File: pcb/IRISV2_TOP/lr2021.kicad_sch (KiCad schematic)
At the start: 52 parts, among them J7 Conn_Coaxial, J8 Conn_Coaxial, U9 lr2021, Y5 ECS-TXO-32CSMV-320-AN-TR

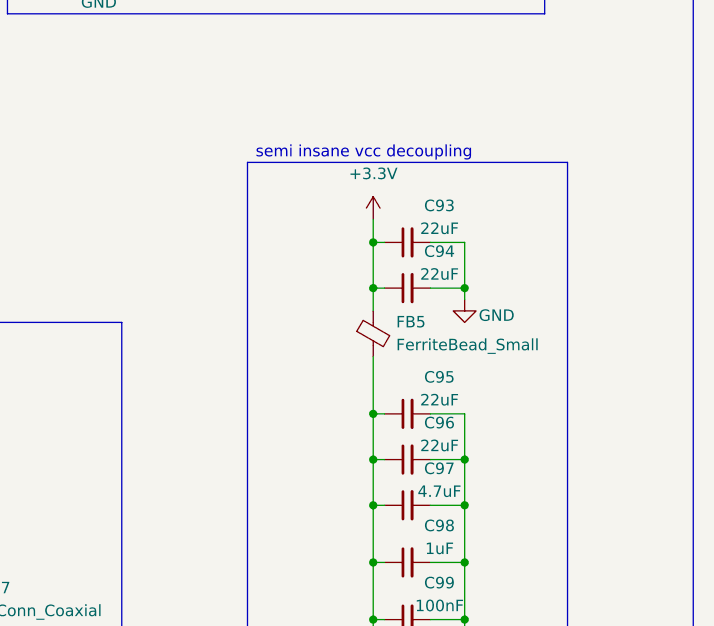
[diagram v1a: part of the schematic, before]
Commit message: removed high g accel, top board layout looking decent, routing started also - though i realized i was missing the micro sd card and that's going to be a pain to add
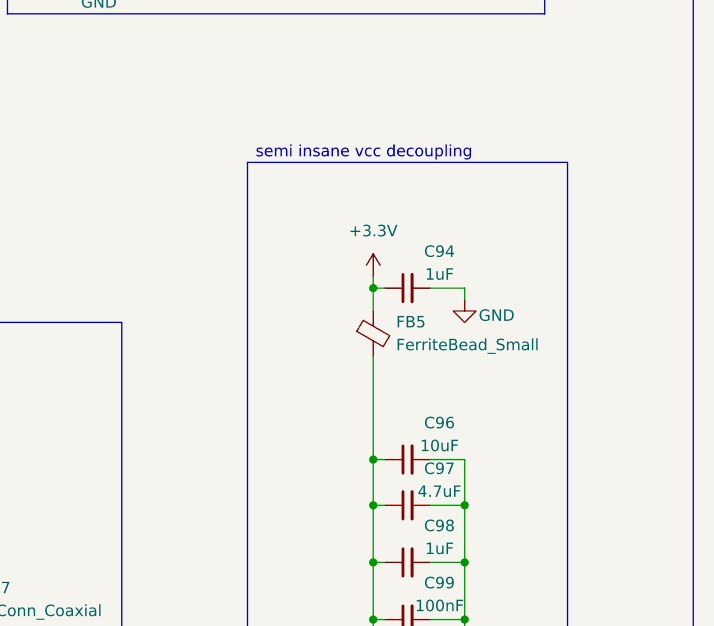
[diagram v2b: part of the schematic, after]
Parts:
- removed C93, C95: 22uF, Capacitor_SMD:C_1210_3225Metric, symbol Device:C_Small
- C80, C81: footprint Capacitor_SMD:C_0805_2012Metric -> Capacitor_SMD:C_0603_1608Metric
- C94: value 22uF -> 1uF; footprint Capacitor_SMD:C_1210_3225Metric -> Capacitor_SMD:C_0603_1608Metric
- C96: value 22uF -> 10uF; footprint Capacitor_SMD:C_1210_3225Metric -> Capacitor_SMD:C_0603_1608Metric
- D7, D8: footprint (none) -> Diode_SMD:D_0201_0603Metric
- FB3, FB4, FB5: footprint (none) -> Inductor_SMD:L_0402_1005Metric

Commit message: layout pretty much done, lr2021 rf stuff done, mostly just routing left
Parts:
- C74, C85: footprint Capacitor_SMD:C_0402_1005Metric -> Capacitor_SMD:C_0201_0603Metric
- J7, J8: footprint (none) -> Connector_Coaxial:U.FL_Hirose_U.FL-R-SMT-1_Vertical
- U9: footprint LR2021:LR2021 -> LR2021:LR2021_thermalvias
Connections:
- net hf: now reaches C92.1, D8.2 (A2), J8.1 (In), L14.2, L15.1
- net hf: no longer C86.2
- net hf_tiein: now reaches C90.2, C91.1, L13.2, L14.1
- net hf_tiein: now also C86.2
- net lf: now reaches C75.2, C82.1, D7.2 (A2), J7.1 (In), L7.2, L9.1
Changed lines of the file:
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@@
 	)
 	(junction
+		(at 119.38 50.8)
+		(diameter 0)
+		(color 0 0 0 0)
+	)
+	(junction
 		(at 119.38 54.61)
 		(diameter 0)
@@
 	(wire
 		(pts
+			(xy 106.68 31.75) (xy 119.38 31.75)
+		)
+		(stroke
+			(width 0)
+			(type default)
+		)
+	)
+	(wire
+		(pts
 			(xy 97.79 31.75) (xy 99.06 31.75)
 		)
@@
 	(wire
 		(pts
-			(xy 129.54 31.75) (xy 129.54 54.61)
-		)
-		(stroke
-			(width 0)
-			(type default)
-		)
-	)
-	(wire
-		(pts
 			(xy 67.31 176.53) (xy 67.31 177.8)
 		)
@@
 	(wire
 		(pts
+			(xy 119.38 31.75) (xy 119.38 50.8)
+		)
+		(stroke
+			(width 0)
+			(type default)
+		)
+	)
+	(wire
+		(pts
 			(xy 138.43 142.24) (xy 139.7 142.24)
 		)
@@
 	(wire
 		(pts
-			(xy 106.68 31.75) (xy 129.54 31.75)
-		)
-		(stroke
-			(width 0)
-			(type default)
-		)
-	)
-	(wire
-		(pts
 			(xy 40.64 35.56) (xy 40.64 36.83)
 		)
@@
 		)
 	)
+	(label "hf"
+		(at 146.05 54.61 0)
+		(effects
+			(font
+				(size 1.27 1.27)
+			)
+			(justify left bottom)
+		)
+	)
 	(label "lfo"
 		(at 25.4 176.53 180)
@@
 		)
 	)
+	(label "lf"
+		(at 83.82 176.53 0)
+		(effects
+			(font
+				(size 1.27 1.27)
+			)
+			(justify left bottom)
+		)
+	)
 	(label "lr2021_vpax"
 		(at 38.1 58.42 90)
@@
 		)
 	)
+	(label "hf_tiein"
+		(at 113.03 31.75 0)
+		(effects
+			(font
+				(size 1.27 1.27)
+			)
+			(justify left bottom)
+		)
+	)
 	(label "lr_vtcxo"
 		(at 24.13 73.66 180)
@@
 			)
 		)
-		(property "Footprint" "Capacitor_SMD:C_0402_1005Metric"
+		(property "Footprint" "Capacitor_SMD:C_0201_0603Metric"
 			(at 36.5252 162.56 0)
 			(effects
@@
 			)
 		)
-		(property "Footprint" ""
+		(property "Footprint" "Connector_Coaxial:U.FL_Hirose_U.FL-R-SMT-1_Vertical"
 			(at 154.94 54.61 0)
 			(effects
@@
 			)
 		)
-		(property "Footprint" "LR2021:LR2021"
+		(property "Footprint" "LR2021:LR2021_thermalvias"
 			(at 60.96 83.82 0)
 			(effects
@@
 			)
 		)
-		(property "Footprint" "Capacitor_SMD:C_0402_1005Metric"
+		(property "Footprint" "Capacitor_SMD:C_0201_0603Metric"
 			(at 98.7552 40.64 0)
 			(effects
@@
 			)
 		)
-		(property "Footprint" ""
+		(property "Footprint" "Connector_Coaxial:U.FL_Hirose_U.FL-R-SMT-1_Vertical"
 			(at 92.71 176.53 0)
 			(effects
